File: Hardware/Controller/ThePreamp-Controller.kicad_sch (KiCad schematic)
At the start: 24 parts, among them J1 8V, J2 Power relay trigger, J3 SPI DISPLAY 1, J4 SPI DISPLAY 2, J5 Digital Out, J6 3.3V (Opt), J8 12V, SW1 RotaryEncoder_Switch, SW2 RotaryEncoder_Switch, U1 TSOP34838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

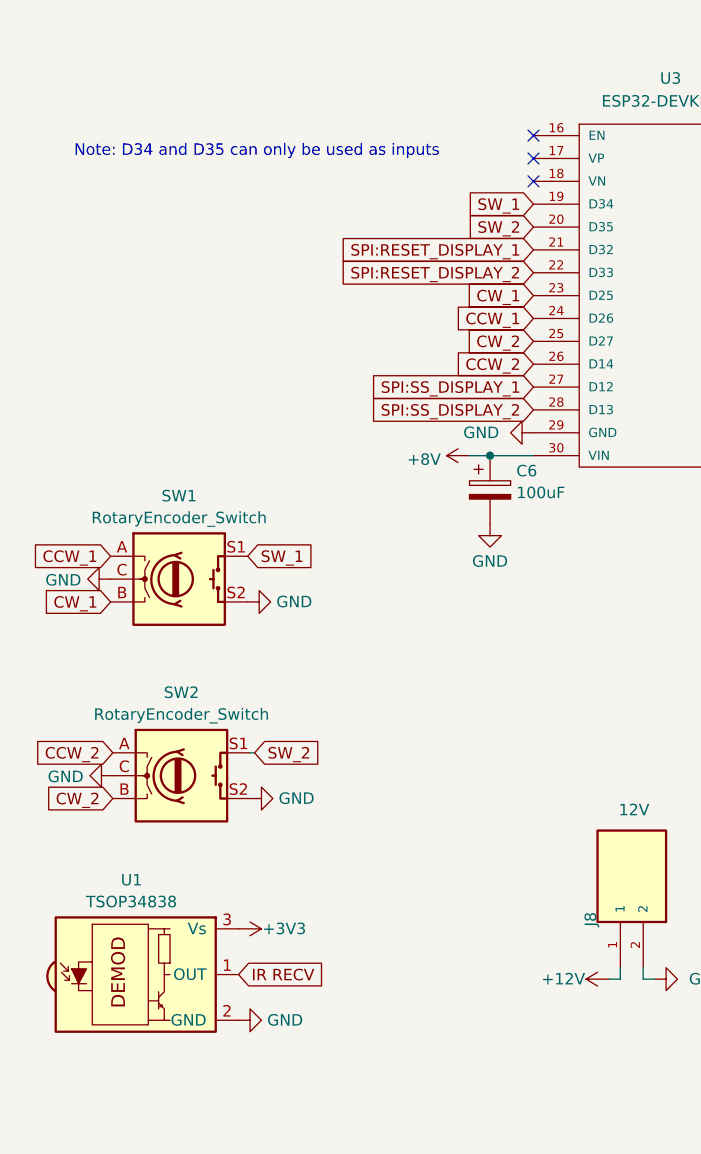
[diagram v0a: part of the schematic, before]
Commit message: Added 10uF for EN pin to stabilize init of displays
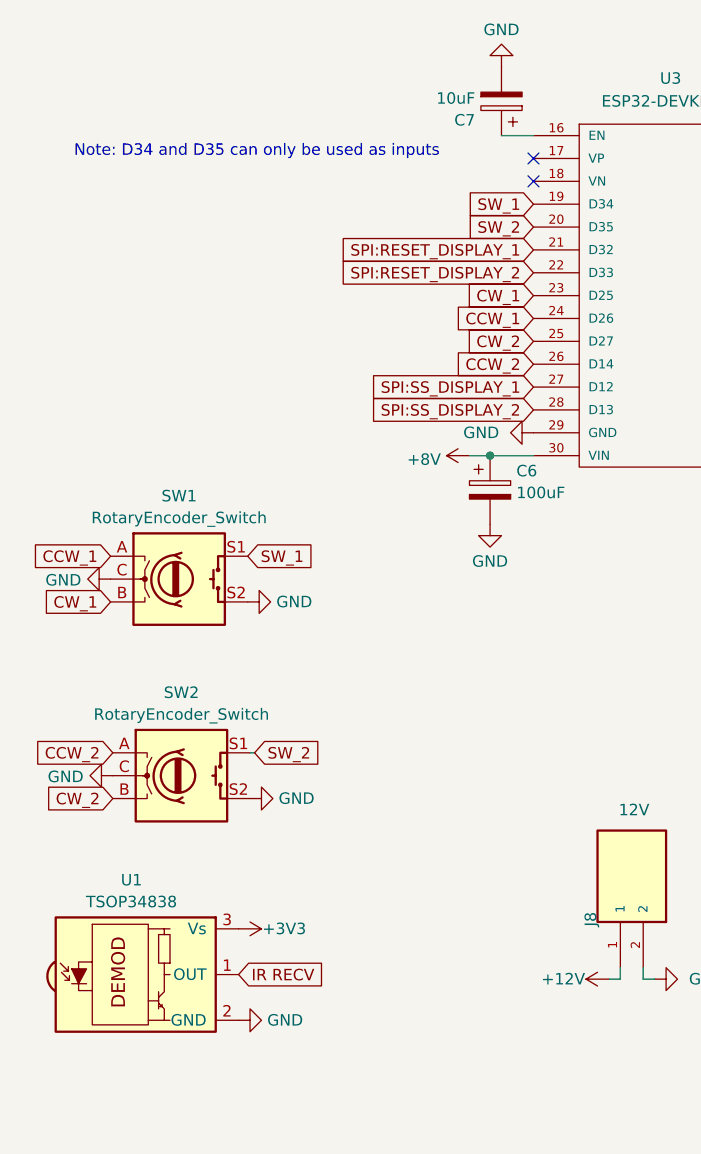
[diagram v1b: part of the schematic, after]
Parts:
- added C7: 10uF, Capacitor_THT:CP_Radial_D8.0mm_P3.50mm, symbol Device:C_Polarized
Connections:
- net GND: now also C7.2
- net at U3.16 (EN): now also C7.1
- no-connect marks 7 -> 6
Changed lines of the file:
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@@
 (kicad_sch
-	(version 20231120)
+	(version 20250114)
 	(generator "eeschema")
-	(generator_version "8.0")
+	(generator_version "9.0")
 	(paper "A4")
+	(text "Note: D34 and D35 can only be used as inputs"
+		(exclude_from_sim no)
+		(at 25.654 34.036 0)
+		(effects
+			(font
+				(size 1.27 1.27)
+			)
+			(justify left bottom)
+		)
+	)
+	(text "https://embeddedthere.com/how-to-design-a-relay-circuit-for-arduino-and-esp32/"
+		(exclude_from_sim no)
+		(at 131.318 53.594 0)
+		(effects
+			(font
+				(size 1.27 1.27)
+			)
+			(justify left bottom)
+		)
+	)
+	(text "Note: D2 can be used to drive a relay (and esp32 built in led will be lit when D2 is high)"
+		(exclude_from_sim no)
+		(at 131.318 50.292 0)
+		(effects
+			(font
+				(size 1.27 1.27)
+			)
+			(justify left bottom)
+		)
+	)
 	(junction
 		(at 236.982 96.266)
@@
 		(at 76.708 34.036)
 	)
-	(no_connect
-		(at 76.708 31.496)
-	)
 	(wire
 		(pts
@@
 	(wire
 		(pts
+			(xy 73.152 31.496) (xy 76.708 31.496)
+		)
+		(stroke
+			(width 0)
+			(type default)
+		)
+	)
+	(wire
+		(pts
 			(xy 30.48 168.91) (xy 30.48 167.64)
 		)
@@
 		)
 	)
-	(text "Note: D34 and D35 can only be used as inputs"
-		(exclude_from_sim no)
-		(at 25.654 34.036 0)
-		(effects
-			(font
-				(size 1.27 1.27)
-			)
-			(justify left bottom)
-		)
-	)
-	(text "https://embeddedthere.com/how-to-design-a-relay-circuit-for-arduino-and-esp32/"
-		(exclude_from_sim no)
-		(at 131.318 53.594 0)
-		(effects
-			(font
-				(size 1.27 1.27)
-			)
-			(justify left bottom)
-		)
-	)
-	(text "Note: D2 can be used to drive a relay (and esp32 built in led will be lit when D2 is high)"
-		(exclude_from_sim no)
-		(at 131.318 50.292 0)
-		(effects
-			(font
-				(size 1.27 1.27)
-			)
-			(justify left bottom)
-		)
-	)
 	(global_label "SW_1"
 		(shape input)
@@
 	)
 	(symbol
+		(lib_id "power:GND")
+		(at 73.152 23.876 0)
+		(mirror x)
+		(unit 1)
+		(exclude_from_sim no)
+		(in_bom yes)
+		(on_board yes)
+		(dnp no)
+		(fields_autoplaced yes)
+		(property "Reference" "#PWR035"
+			(at 73.152 17.526 0)
+			(effects
+				(font
+					(size 1.27 1.27)
+				)
+				(hide yes)
+			)
+		)
+		(property "Value" "GND"
+			(at 73.152 19.7429 0)
+			(effects
+				(font
+					(size 1.27 1.27)
+				)
+			)
+		)
+		(property "Footprint" ""
+			(at 73.152 23.876 0)
+			(effects
+				(font
+					(size 1.27 1.27)
+				)
+				(hide yes)
+			)
+		)
+		(property "Datasheet" ""
+			(at 73.152 23.876 0)
+			(effects
+				(font
+					(size 1.27 1.27)
+				)
+				(hide yes)
+			)
+		)
+		(property "Description" ""
+			(at 73.152 23.876 0)
+			(effects
+				(font
+					(size 1.27 1.27)
+				)
+				(hide yes)
+			)
+		)
+		(pin "1"
+		)
+		(instances
+			(project "ThePreamp-Controller"
+				(path "/f6c644f4-3036-41a6-9e14-2c08c079c6cd"
+					(reference "#PWR035")
+					(unit 1)
+				)
+			)
+		)
+	)
+	(symbol
 		(lib_id "Device:C")
 		(at 240.792 159.004 90)
@@
 	)
 	(symbol
+		(lib_id "Device:C_Polarized")
+		(at 73.152 27.686 180)
+		(unit 1)
+		(exclude_from_sim no)
+		(in_bom yes)
+		(on_board yes)
+		(dnp no)
+		(fields_autoplaced yes)
+		(property "Reference" "C7"
+			(at 70.231 29.7872 0)
+			(effects
+				(font
+					(size 1.27 1.27)
+				)
+				(justify left)
+			)
+		)
+		(property "Value" "10uF"
+			(at 70.231 27.3629 0)
+			(effects
+				(font
+					(size 1.27 1.27)
+				)
+				(justify left)
+			)
+		)
+		(property "Footprint" "Capacitor_THT:CP_Radial_D8.0mm_P3.50mm"
+			(at 72.1868 23.876 0)
+			(effects
+				(font
+					(size 1.27 1.27)
+				)
+				(hide yes)
+			)
+		)
+		(property "Datasheet" "~"
+			(at 73.152 27.686 0)
+			(effects
+				(font
+					(size 1.27 1.27)
+				)
+				(hide yes)
+			)
+		)
+		(property "Description" "Polarized capacitor"
+			(at 73.152 27.686 0)
+			(effects
+				(font
+					(size 1.27 1.27)
+				)
+				(hide yes)
+			)
+		)
+		(pin "2"
+		)
+		(pin "1"
+		)
+		(instances
+			(project "ThePreamp-Controller"
+				(path "/f6c644f4-3036-41a6-9e14-2c08c079c6cd"
+					(reference "C7")
+					(unit 1)
+				)
+			)
+		)
+	)
+	(symbol
 		(lib_id "power:+3.3V")
 		(at 215.138 33.02 270)
@@
 		)
 	)
+	(embedded_fonts no)
 )
